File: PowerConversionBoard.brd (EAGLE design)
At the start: 152.4 x 97.2 mm, 48 parts, among them U1 LM2678, U2 LM2678

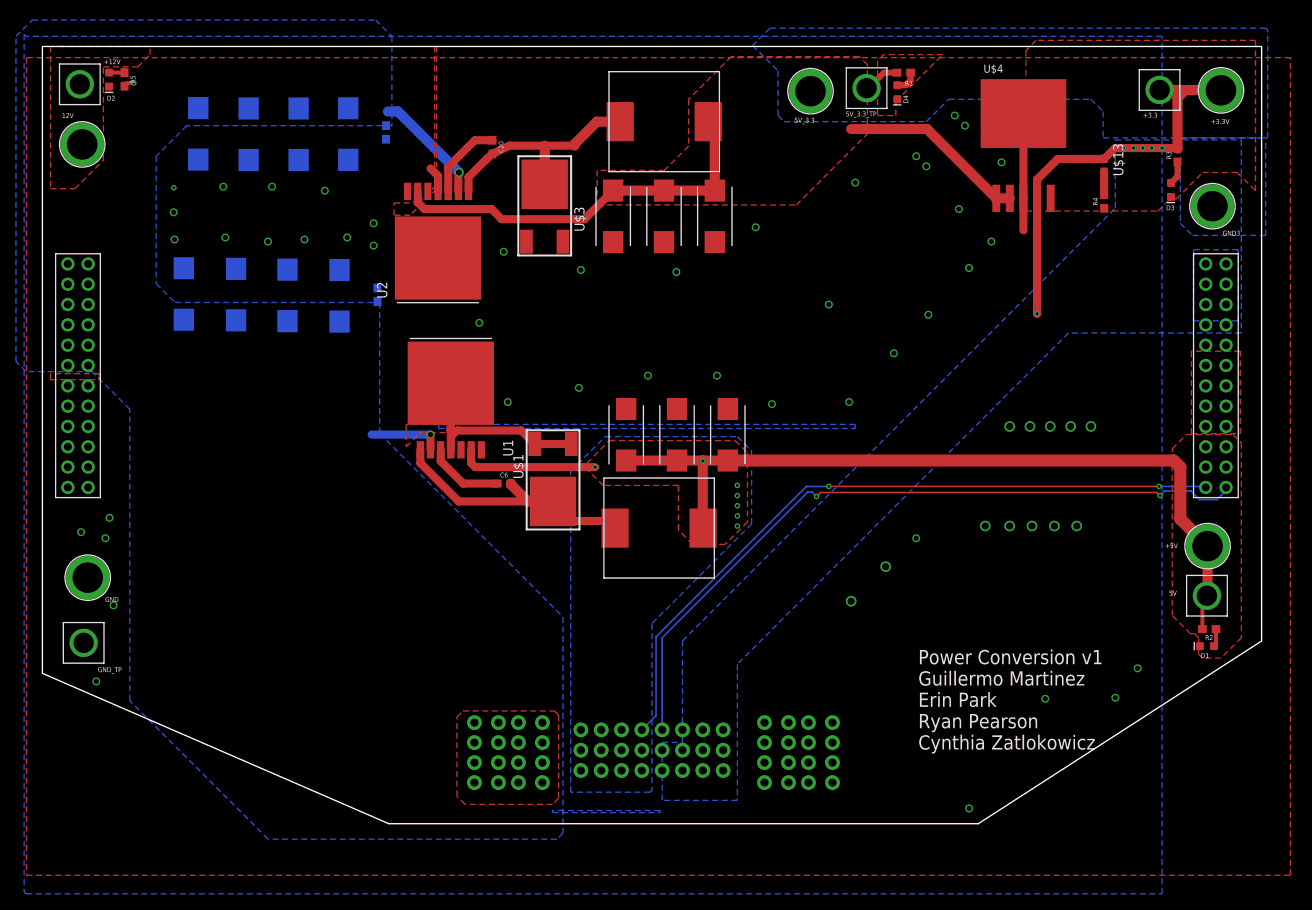
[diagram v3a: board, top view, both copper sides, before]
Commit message: stupid outline. extra breakouts. tighter layout.
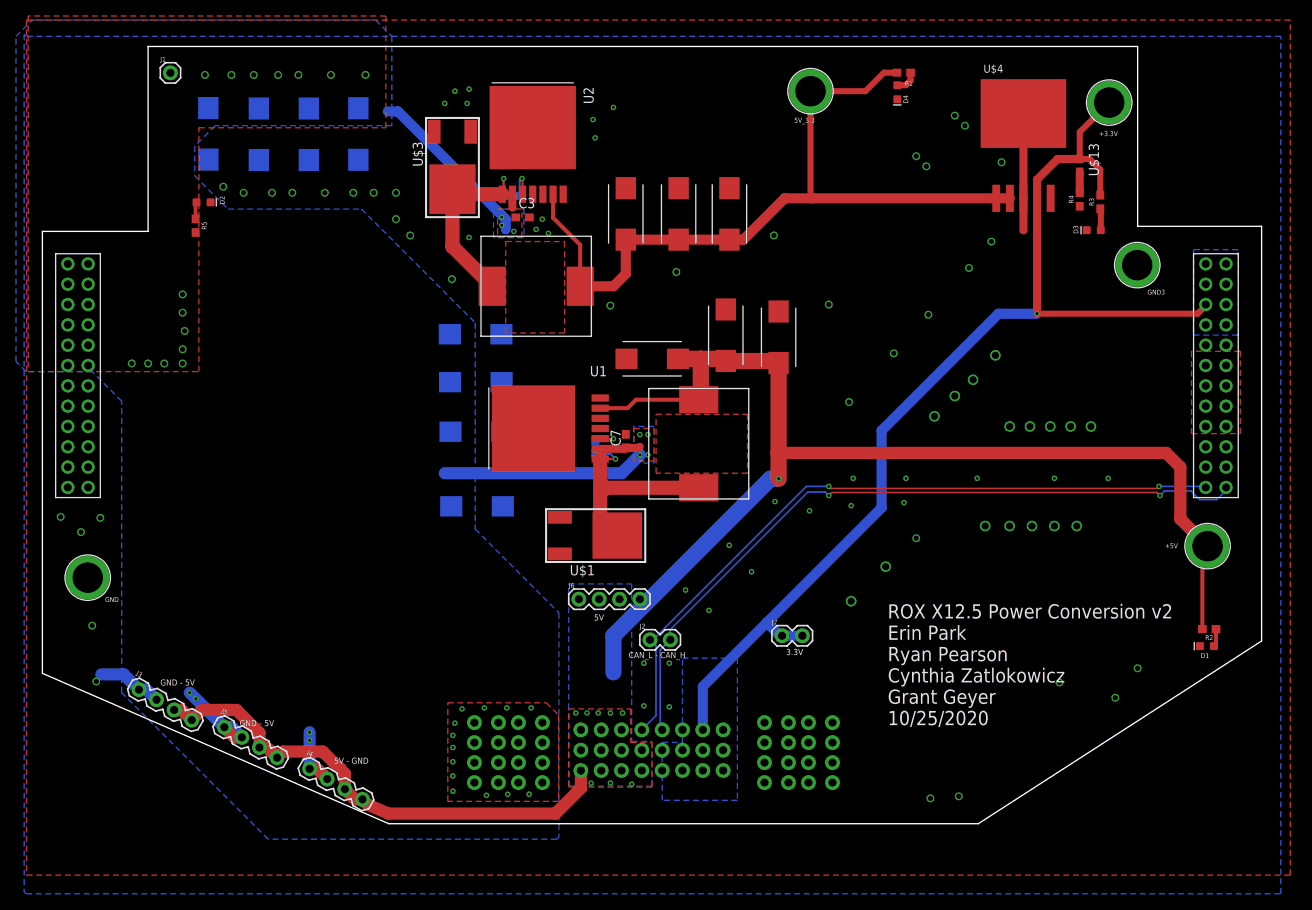
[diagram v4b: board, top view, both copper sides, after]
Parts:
- removed +12V, +3.3, 5V, 5V_3.3_TP, GND_TP: TP, TP:TP
- removed 12V: (no value), SparkFun-Connectors:BANANA_CONN
- added J1: (no value), SparkFun-Connectors:1X01
- added J2, J7: (no value), SparkFun-Connectors:1X02
- added J3, J4, J5, J6: (no value), SparkFun-Connectors:1X04
- moved C16 40.1 mm to (54.3, 44.1), turned to 180 degrees
- moved C15 36.8 mm to (54.2, 65.6), turned to 180 degrees
- moved C7 36.0 mm to (72.9, 52.3), flipped to the top
- moved C17 29.1 mm to (54.2, 53.4), turned to 180 degrees
- moved U$6 26.1 mm to (61.7, 71.6)
- moved R5 20.3 mm to (19.2, 79.2)
- moved C18 20.2 mm to (54.2, 59.6), turned to 180 degrees
- moved U2 20.1 mm to (61.3, 91.5), turned to 270 degrees
- moved C3 20.1 mm to (60.0, 80.2), flipped to the top, turned to 0 degrees
- moved D2 19.4 mm to (20.1, 82.1), turned to 0 degrees
- moved +3.3V 14.1 mm to (133.3, 94.6)
- moved C10 13.9 mm to (85.4, 65.5)
- moved C12 13.7 mm to (92.0, 65.3)
- moved U$3 12.8 mm to (51.3, 86.9), turned to 90 degrees
- moved C6 12.3 mm to (69.1, 51.5), flipped to the bottom, turned to 270 degrees
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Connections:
- net N$1 renamed SW_5
- net N$2 renamed BST_5_3
- net N$3 renamed BST
- net N$7 renamed SW_5_3
- net +12V: now also J1.1; no longer +12V.P$1, 12V.P$1
- net +3.3V: now also J7.1, J7.2; no longer +3.3.P$1
- net +5V: now also J3.3, J3.4, J4.3, J4.4, J5.3, J5.4, J6.1, J6.2, J6.3, J6.4; no longer 5V.P$1
- net +5V_3.3V: no longer 5V_3.3_TP.P$1
- net CAN_H: now also J2.2
- net CAN_L: now also J2.1
- net GND: now also J3.1, J3.2, J4.1, J4.2, J5.1, J5.2; no longer GND_TP.P$1
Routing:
- net +5V: track 115.4 -> 214.8 mm, vias 7 -> 9
- net +3.3V: track 51.5 -> 137.0 mm, vias 6 -> 1
- net +12V: track 25.0 -> 53.6 mm, vias 3 -> 35
- net +5V_3.3V: track 77.5 -> 98.9 mm
- net SW_5: track 36.6 -> 28.3 mm, vias 0 -> 1
- net BST_5_3: track 9.97 -> 4.27 mm, vias 0 -> 1
- net BST: track 9.64 -> 4.00 mm, vias 0 -> 1
- net SW_5_3: track 28.3 -> 26.0 mm, vias 0 -> 1
- net GND: track 42.8 -> 44.9 mm, vias 57 -> 84
- net CAN_L: track 88.9 -> 90.0 mm
- added copper zone on layer 1, net +12V
- added copper zone on layer 1, net X
- removed copper zone on layer 1, net +5V_3.3V
- removed copper zone on layer 1, net CUT
- removed copper zone on layer 16, net CUT
- removed copper zone on layer 16, net CUTG
- removed copper zone on layer 1, net GNDCUT
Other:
- outline, holes or cut-outs redrawn
- board text added: "3.3V"
- board text added: "5V"
- board text added: "5V - GND"
- board text added: "CAN_L - CAN_H"
- board text added: "GND - 5V"
- board text added: "ROX X12.5 Power Conversion v2 Erin Park Ryan Pearson Cynthia Zatlokowicz Grant Geyer 10/25/2020"
- board text removed: "Power Conversion v1 Guillermo Martinez Erin Park Ryan Pearson Cynthia Zatlokowicz"
